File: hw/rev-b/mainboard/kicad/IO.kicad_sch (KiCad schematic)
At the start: 7 parts, among them U11 W65C21N, U12 W65C21N, U13 W65C22N

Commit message: hw: repurpose SP0 (spare) for independent VSYNC
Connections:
- net BVERT renamed BVSYNC
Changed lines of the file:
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@@
 		)
 	)
-	(hierarchical_label "BVERT"
+	(hierarchical_label "BVSYNC"
 		(shape input)
 		(at 240.03 68.58 0)

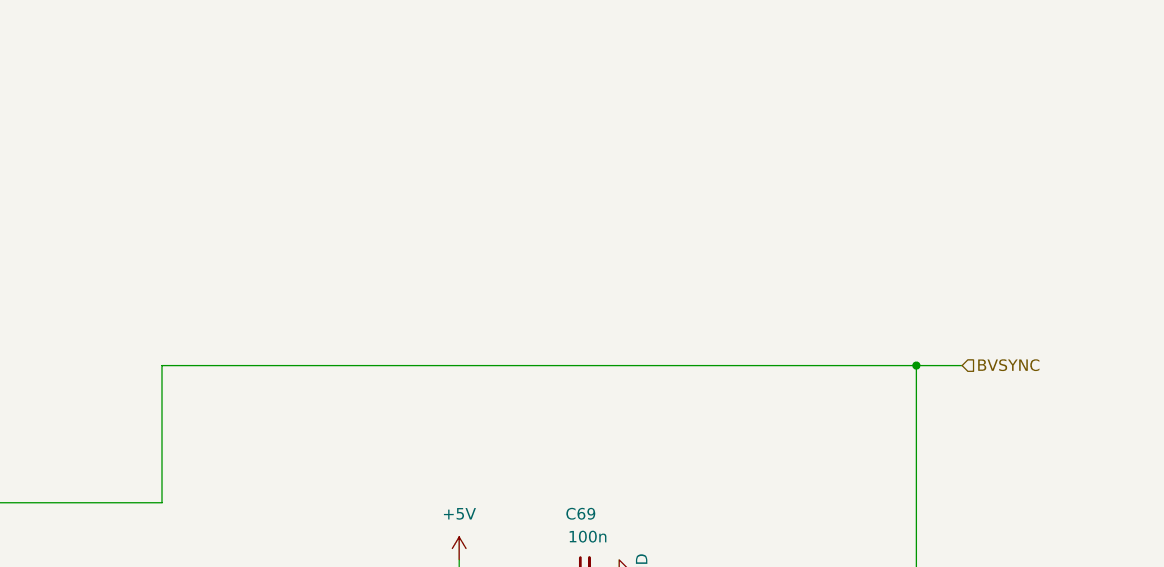
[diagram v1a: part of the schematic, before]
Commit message: hw: audio_det, stitching around sram
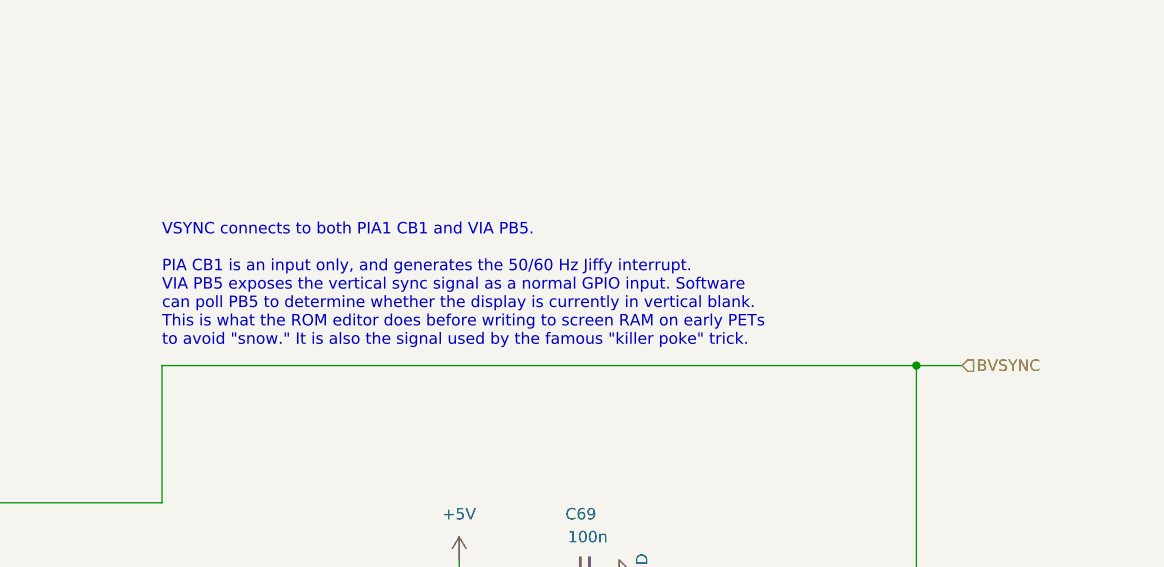
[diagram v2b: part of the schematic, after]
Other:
- note added: "VSYNC connects to both PIA1 CB1 and VIA PB5. PIA CB1 is an input only, and generates the 50/60 Hz Jiffy interrupt. VIA PB5 exposes the vertical sync signal as a normal GPIO input. Software can poll PB5 to determine whether the display is currently in vertical blank. This is what the ROM editor does before writing to screen RAM on early PETs to avoid "snow." It is also the signal used by the famou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"
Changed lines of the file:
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@@
+		)
+	)
+	(text "VSYNC connects to both PIA1 CB1 and VIA PB5.\n\nPIA CB1 is an input only, and generates the 50/60 Hz Jiffy interrupt.\nVIA PB5 exposes the vertical sync signal as a normal GPIO input. Software\ncan poll PB5 to determine whether the display is currently in vertical blank.\nThis is what the ROM editor does before writing to screen RAM on early PETs\nto avoid \"snow.\" It is also the signal used by the famous \"killer poke\" trick."
+		(exclude_from_sim no)
+		(at 151.13 59.69 0)
+		(effects
+			(font
+				(size 1.27 1.27)
+			)
+			(justify left)
 		)
 	)
